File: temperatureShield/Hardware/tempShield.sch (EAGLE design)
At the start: 4 parts

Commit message: still work on the schematic
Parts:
- removed LCD1: (no value), Particle:LCD
- added C1: 0.1uF, SparkFun-Capacitors:0.22UF50V-20%,+80%(0603)
- added J1: ADAFRUIT2_1X2-3.5MM, asset-tracker-v007:ADAFRUIT2_1X2-3.5MM
- added R1, R11, R2, R3, R4, R5, R6: 10k, SparkFun-Resistors:0.27OHM-1/10W-1%(0603)
- added R10, R12, R13, R14, R15, R16, R7, R8, R9: 100K, programming-rig-v402:R-US_R0402
- added S1: (no value), Particle:TAC_SWITCHSMD
- added U$1: MICROBUILDER_ELECTRON_SMT, asset-tracker-v007:MICROBUILDER_ELECTRON_SMT
- added U$2: PARTICLE-DEVICES_ELECTRON_WITH_STACKABLE_HEADERS, fuelview_v001:PARTICLE-DEVICES_ELECTRON_WITH_STACKABLE_HEADERS
- added U3: FUJITSU_MB85RS1MT, fuelview_v001:FUJITSU_MB85RS1MT
- added U4: (no value), Particle:LCD
- U1: value (none) -> SHT30; device Particle:SHT30 -> Particle:SHT30SHT30
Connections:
- new net !ALERT: R11.1, U2.!ALERT!
- new net !CS: R2.1, U3.!CS
- new net !HOLD: R4.1, U3.!HOLD
- new net +3V3: C1.2, R10.2, R11.2, R2.2, R3.2, R4.2, R5.2, R6.2, R7.2, R8.2, R9.2, U1.VDD, U2.VCC, U3.VDD
- new net ALERT: R6.1, U1.ALERT
- new net COM1: R10.1, R15.2, U4.COM1
- new net COM2: R14.2, R9.1, U4.COM2
- new net COM3: R13.2, R8.1, U4.COM3
- new net COM4: R12.2, R7.1, U4.COM4
- new net D0: U4.A
- new net D1: U4.B
- new net D2: U4.F
- new net D3: U4.G
- new net D4: U4.C
- new net D5: U4.E
- new net D6: U4.D
- new net D7: U4.P
- new net GND: C1.1, R12.1, R13.1, R14.1, R15.1, U1.ADDR, U1.PAD, U1.R, U1.VSS, U2.ADR0, U2.ADR1, U2.AGND, U2.DGND, U3.VSS
- new net MISO: U3.SO
- new net MOSI: U3.SI
- new net N$2: R3.1, U3.!WP
- new net RESET: R5.1, U1.NRESET
- new net SCK: U3.SCK
- new net SCL: U1.SCL, U2.SCL
- new net SDA: U1.SDA, U2.SDA
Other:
- note added: "I2C Address=0X44"
- note added: "I2C Address=0X80"
- moved on the sheet: U$3

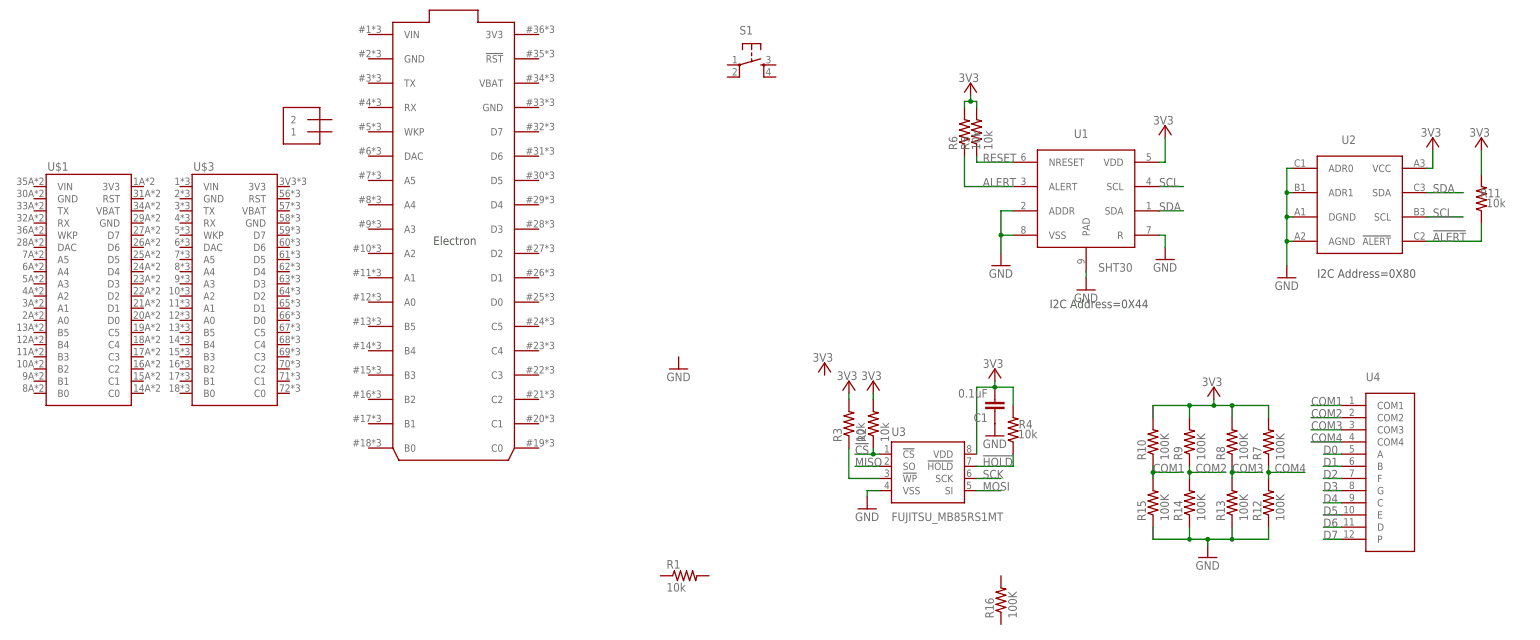
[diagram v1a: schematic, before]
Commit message: finished the schematic and part of the layout
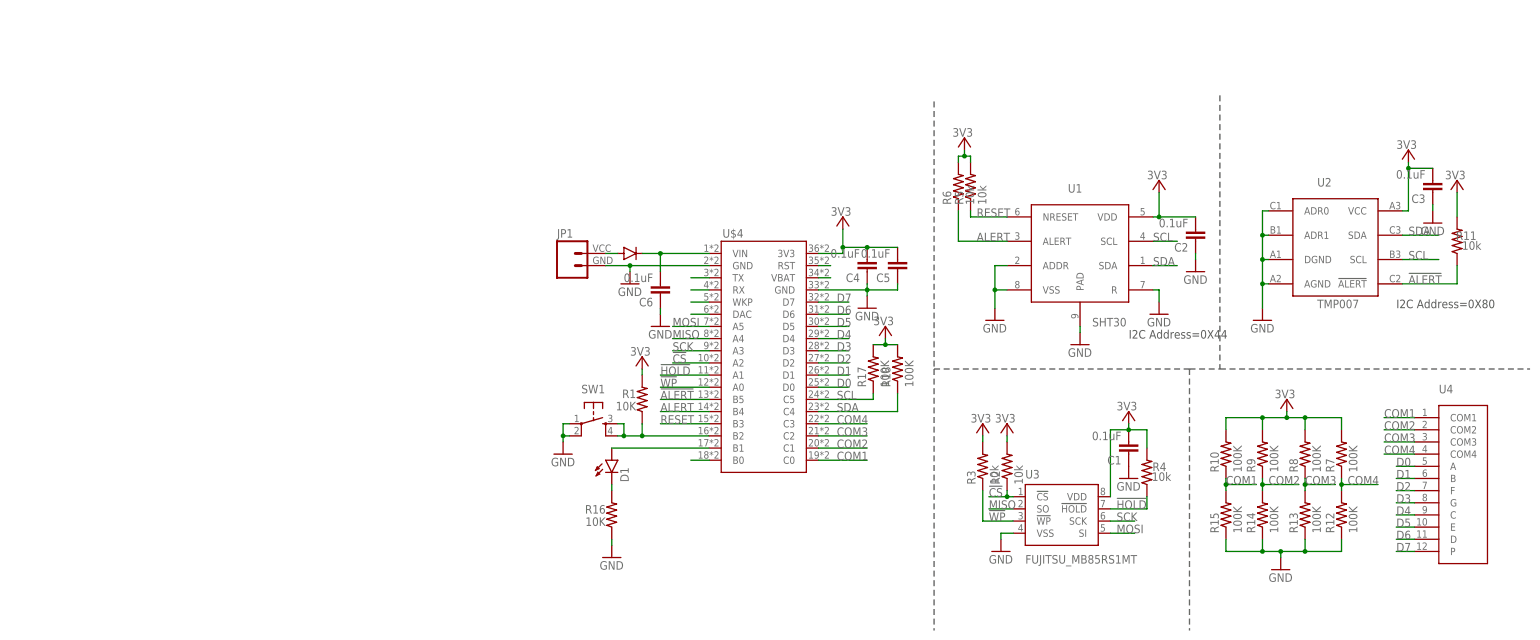
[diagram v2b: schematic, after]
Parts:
- removed J1: ADAFRUIT2_1X2-3.5MM, asset-tracker-v007:ADAFRUIT2_1X2-3.5MM
- removed S1: (no value), Particle:TAC_SWITCHSMD
- removed U$2: PARTICLE-DEVICES_ELECTRON_WITH_STACKABLE_HEADERS, fuelview_v001:PARTICLE-DEVICES_ELECTRON_WITH_STACKABLE_HEADERS
- removed U$3: ELECTRONDUALROW, Particle:ELECTRONDUALROW
- added C2, C3, C4, C5, C6: 0.1uF, SparkFun-Capacitors:0.22UF50V-20%,+80%(0603)
- added D1: (no value), SparkFun-LED:LED0603
- added JP1: (no value), electron_v020:SPARKFUN-CONNECTORS_M024UCON-15767
- added R17, R18: 100K, programming-rig-v402:R-US_R0402
- added SW1: (no value), SparkFun-Electromechanical:SWITCH_SPST_4_PIN
- added U$4: MICROBUILDER_ELECTRON_SMT, asset-tracker-v007:MICROBUILDER_ELECTRON_SMT
- R1: value 10k -> 10K; device SparkFun-Resistors:0.27OHM-1/10W-1%(0603) -> programming-rig-v402:R-US_R0402
- R16: value 100K -> 10K
- U$1: value MICROBUILDER_ELECTRON_SMT -> PARTICLE_DIODE_NT; device asset-tracker-v007:MICROBUILDER_ELECTRON_SMT -> electron_v020:PARTICLE_DIODE_NT
- U2: value (none) -> TMP007
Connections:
- new net !WP: R3.1, U$4.A0, U3.!WP
- new net N$1: C6.2, U$1.CATHODE, U$4.VIN
- new net N$10: U$4.WKP
- new net N$11: U$4.DAC
- new net N$12: U$4.B0
- new net N$3: JP1.2, U$1.ANODE
- new net N$4: R1.1, SW1.3, SW1.4, U$4.B2
- new net N$5: D1.C, R16.2
- new net N$6: U$4.RST
- new net N$7: U$4.VBAT
- new net N$8: U$4.TX
- new net N$9: U$4.RX
- net !ALERT: now also U$4.B5
- net !CS: now also U$4.A2
- net !HOLD: now also U$4.A1
- net +3V3: now also C2.2, C3.2, C4.2, C5.2, R1.2, R17.2, R18.2, U$4.3V3
- net ALERT: now also U$4.B4
- net COM1: now also U$4.C0
- net COM2: now also U$4.C1
- net COM3: now also U$4.C2
- net COM4: now also U$4.C3
- net D0: now also U$4.D0
- net D1: now also U$4.D1
- net D2: now also U$4.D2
- net D3: now also U$4.D3
- net D4: now also U$4.D4
- net D5: now also U$4.D5
- net D6: now also U$4.D6
- net D7: now also U$4.D7
- net GND: now also C2.1, C3.1, C4.1, C5.1, C6.1, JP1.1, R16.1, SW1.1, SW1.2, U$4.GND, U$4.GND@2
- net MISO: now also U$4.A4
- net MOSI: now also U$4.A5
- net N$2: now also D1.A, U$4.B1; no longer R3.1, U3.!WP
- net RESET: now also U$4.B3
- net SCK: now also U$4.A3
- net SCL: now also R17.1, U$4.C5
- net SDA: now also R18.1, U$4.C4
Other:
- moved on the sheet: C1, R1, R10, R11, R12, R13, R14, R15, R16, R2, R3, R4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
